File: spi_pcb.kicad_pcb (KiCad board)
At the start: 2 copper layers, 65 x 56 mm, 20 parts, among them J1 GPIO, J2 PWR, U1 LMZ23605TZ

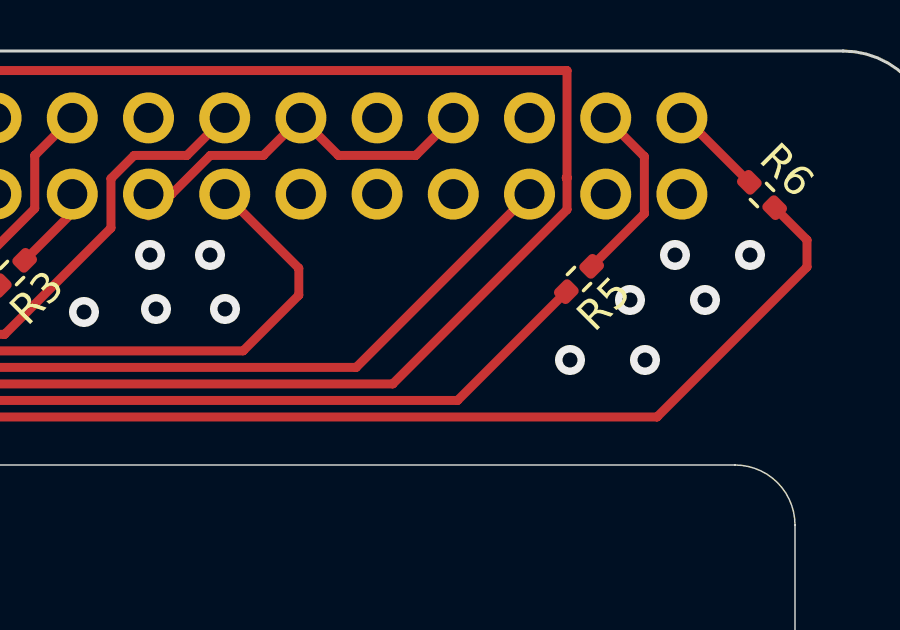
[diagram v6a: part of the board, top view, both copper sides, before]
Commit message: Fill all areas with copper to reduce CNC time.
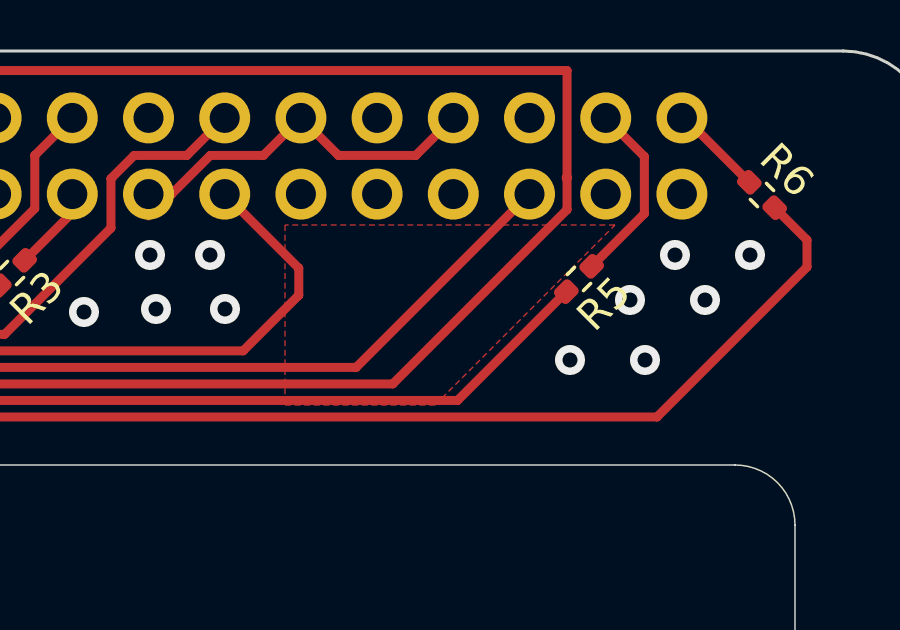
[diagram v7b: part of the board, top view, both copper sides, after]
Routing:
- added copper zone on F.Cu, net (none)
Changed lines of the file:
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@@
+	)
+	(zone
+		(net 0)
+		(net_name "")
+		(layer "F.Cu")
+		(name "fill")
+		(hatch none 0.5)
+		(priority 1)
+		(connect_pads yes
+			(clearance 0.5)
+		)
+		(min_thickness 0.25)
+		(filled_areas_thickness no)
+		(fill yes
+			(thermal_gap 0.5)
+			(thermal_bridge_width 0.5)
+			(island_removal_mode 1)
+			(island_area_min 10)
+		)
+		(polygon
+			(pts
+				(xy 143.4 49.8) (xy 143.4 55.8) (xy 148.4 55.8) (xy 154.4 49.8)
+			)
+		)
 	)
 	(zone

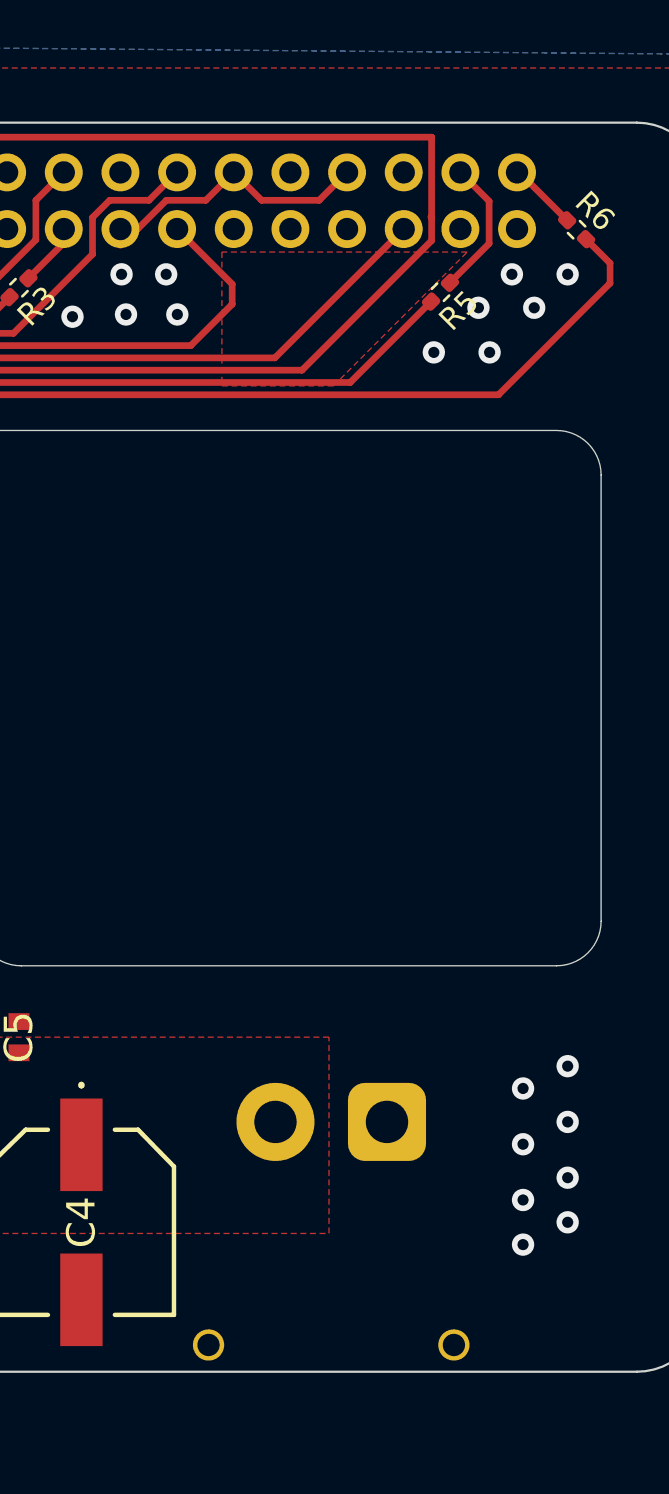
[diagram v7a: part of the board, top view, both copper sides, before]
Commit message: Move power connector a bit closer to centre. Add project library.
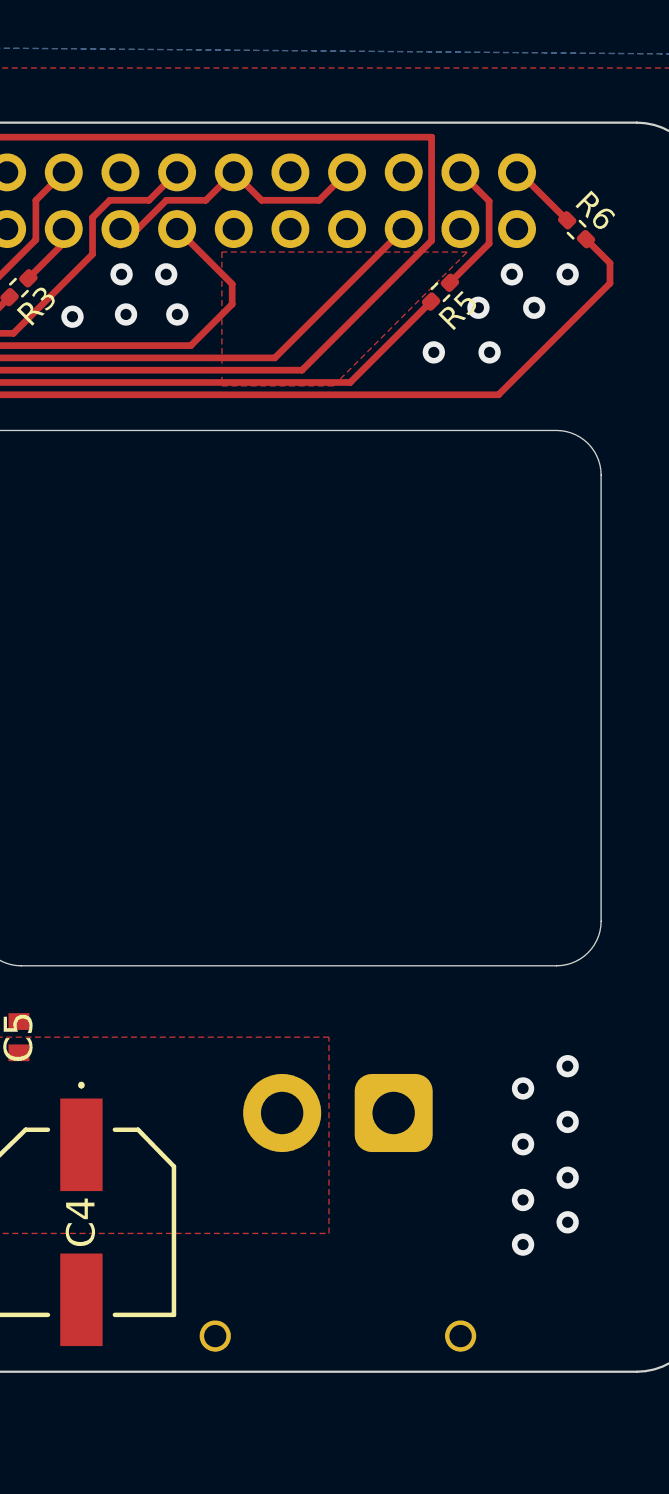
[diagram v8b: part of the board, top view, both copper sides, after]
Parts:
- C1: footprint Kicad Library:EEFCX0J101R -> imported:EEFCX0J101R
- C2: footprint Kicad Library:CAPC3216X180N -> imported:CAPC3216X180N
- C3, C5: footprint Kicad Library:CAPC1608X90N -> imported:CAPC1608X90N
- C4: footprint Kicad Library:16SVPT560M -> imported:16SVPT560M
- U1: value LMZ23605TZ -> imported:LMZ23605TZ
- moved J2 0.50 mm to (151.1, 88.4)
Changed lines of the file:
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@@
 	(net 41 "Net-(SPI2-Pin_3)")
 	(net 42 "Net-(SPI2-Pin_5)")
-	(footprint "Kicad Library:EEFCX0J101R"
+	(footprint "imported:EEFCX0J101R"
 		(layer "F.Cu")
 		(at 117.5 83.1 -90)
@@
 		)
 	)
-	(footprint "Kicad Library:CAPC3216X180N"
+	(footprint "imported:CAPC3216X180N"
 		(layer "F.Cu")
 		(at 122 82.7 90)
@@
 		)
 	)
-	(footprint "Kicad Library:CAPC1608X90N"
+	(footprint "imported:CAPC1608X90N"
 		(layer "F.Cu")
 		(at 132.7 85 90)
@@
 			)
 		)
-		(property "Value" "LMZ23605TZ"
+		(property "Value" "imported:LMZ23605TZ"
 			(at 0 6.33 90)
 			(layer "F.Fab")
@@
 		)
 	)
-	(footprint "Kicad Library:16SVPT560M"
+	(footprint "imported:16SVPT560M"
 		(layer "F.Cu")
 		(at 137.1 93.3 -90)
@@
 		)
 	)
-	(footprint "Kicad Library:CAPC1608X90N"
+	(footprint "imported:CAPC1608X90N"
 		(layer "F.Cu")
 		(at 134.3 85 90)
@@
 	(footprint "Connector_AMASS:AMASS_XT30PW-M_1x02_P2.50mm_Horizontal"
 		(layer "B.Cu")
-		(at 150.8 88.8)
+		(at 151.1 88.4)
 		(descr "Connector XT30 Horizontal PCB Male, https://www.tme.eu/Document/6eb2005a51a52592b3f19e8a450c54c8/XT30PW-M.pdf")
 		(tags "RC Connector XT30")
@@
 	)
 	(segment
-		(start 152.801 48.251818)
-		(end 152.774591 48.225409)
-		(width 0.3)
-		(layer "F.Cu")
-		(net 8)
-	)
-	(segment
-		(start 152.801 49.288182)
-		(end 152.801 48.251818)
-		(width 0.3)
-		(layer "F.Cu")
-		(net 8)
-	)
-	(segment
-		(start 152.801 48.199)
-		(end 152.801 44.651)
-		(width 0.3)
-		(layer "F.Cu")
-		(net 8)
-	)
-	(segment
-		(start 122.649 44.651)
-		(end 121.07 46.23)
-		(width 0.3)
-		(layer "F.Cu")
-		(net 8)
-	)
-	(segment
 		(start 118.057 72.072228)
 		(end 118.057 59.056088)
@@
 	)
 	(segment
-		(start 152.774591 48.225409)
-		(end 152.801 48.199)
+		(start 122.649 44.651)
+		(end 121.07 46.23)
 		(width 0.3)
 		(layer "F.Cu")
@@
 	)
 	(segment
-		(start 152.801 44.651)
-		(end 122.649 44.651)
+		(start 111.78 88.05)
+		(end 112.28 88.05)
 		(width 0.3)
 		(layer "F.Cu")
@@
 	)
 	(segment
+		(start 152.801 44.651)
+		(end 122.649 44.651)
+		(width 0.3)
+		(layer "F.Cu")
+		(net 8)
+	)
+	(segment
 		(start 146.991566 55.097616)
 		(end 152.801 49.288182)
@@
 	)
 	(segment
-		(start 118.057 59.056088)
-		(end 122.015472 55.097616)
+		(start 152.801 49.288182)
+		(end 152.801 44.651)
 		(width 0.3)
 		(layer "F.Cu")
@@
 	)
 	(segment
-		(start 111.78 88.05)
-		(end 112.28 88.05)
+		(start 118.057 59.056088)
+		(end 122.015472 55.097616)
 		(width 0.3)
 		(layer "F.Cu")
@@
 	)
 	(segment
-		(start 111.78 88.1)
-		(end 112.03 88.1)
+		(start 114.298 77.710464)
+		(end 114.302 77.706464)
 		(width 0.3)
 		(layer "F.Cu")
@@
 	)
 	(segment
-		(start 114.302 75.827228)
-		(end 118.057 72.072228)
+		(start 111.78 88.1)
+		(end 112.03 88.1)
 		(width 0.3)
 		(layer "F.Cu")
@@
 	)
 	(segment
-		(start 114.298 77.710464)
-		(end 114.302 77.706464)
+		(start 114.302 75.827228)
+		(end 118.057 72.072228)
 		(width 0.3)
 		(layer "F.Cu")
